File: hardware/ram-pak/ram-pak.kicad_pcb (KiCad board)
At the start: 4 copper layers, 29 x 18.1 mm, 23 parts, among them J1 PinHeader_2x22_P1.27mm, U1 TLV62568DBV, U2 S70KL1281, U3 S70KL1281

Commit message: Added missing 3d models.
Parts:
- J1: footprint pkl_pin_headers:PinHeader_2x22_P1.27mm_Vertical_Pass-Through__SMD -> pkl_pin_sockets:PinSocket_2x22_P1.27mm_Vertical_Pass-Through__SMD

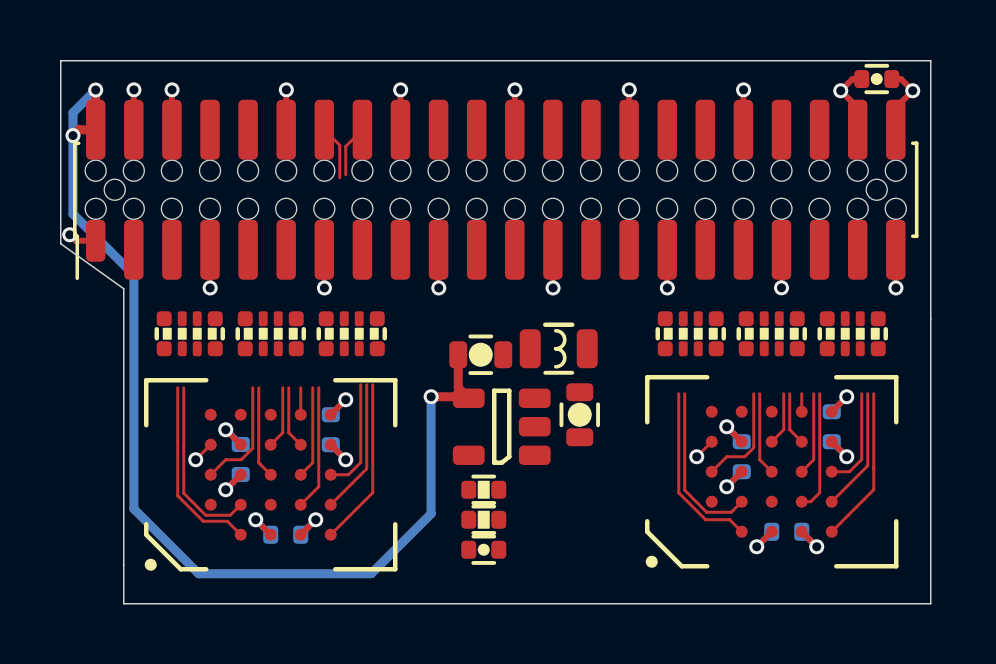
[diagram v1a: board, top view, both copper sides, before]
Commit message: Ram-Pak: Routed and length matched.
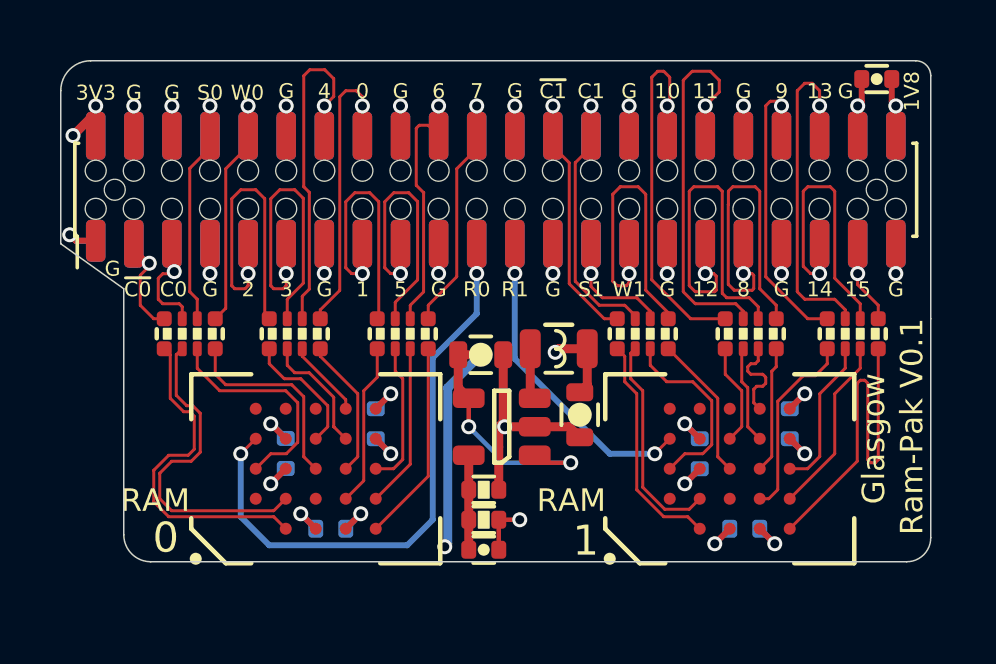
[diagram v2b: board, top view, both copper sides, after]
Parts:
- moved R3 1.70 mm to (36.9, 34.8)
- moved R4 1.60 mm to (44.9, 34.8)
- moved C5 1.51 mm to (34.5, 41.3)
- moved C6 1.51 mm to (36.0, 37.8)
- moved C7 1.51 mm to (33.0, 38.8)
- moved U2 1.51 mm to (34.0, 39.3)
- moved C10 1.40 mm to (46.8, 38.8)
- moved C8 1.40 mm to (48.3, 41.3)
- moved C9 1.40 mm to (49.8, 37.8)
- moved U3 1.40 mm to (47.8, 39.3)
- moved R2 0.80 mm to (33.3, 34.8)
- moved R5 0.70 mm to (48.5, 34.8)
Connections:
- net /CK0 renamed /CK0_P
- net /CK1 renamed /CK1_P
- net /Z0_N renamed /DQ15x
- net /Z0_P renamed /DQ14x
- net /Z10_N renamed /DQ3x
- net /Z10_P renamed /DQ2x
- net /Z11_N renamed /CK0x_N
- net /Z11_P renamed /CK0x_P
- net /Z12_N renamed /RWDS0x
- net /Z12_P renamed /~CS0x
- net /Z1_N renamed /DQ9x
- net /Z1_P renamed /DQ13x
- net /Z2_N renamed /DQ12x
- net /Z2_P renamed /DQ8x
- net /Z3_N renamed /RWDS1x
- net /Z3_P renamed /~CS1x
- net /Z4_N renamed /DQ11x
- net /Z4_P renamed /DQ10x
- net /Z5_N renamed /CK1x_N
- net /Z5_P renamed /CK1x_P
- net /Z6_N renamed /~RESET1
- net /Z6_P renamed /~RESET0
- net /Z7_N renamed /DQ6x
- net /Z7_P renamed /DQ7x
- net /Z8_N renamed /DQ5x
- net /Z8_P renamed /DQ1x
- net /Z9_N renamed /DQ4x
- net /Z9_P renamed /DQ0x
- net /~CK0 renamed /CK0_N
- net /~CK1 renamed /CK1_N
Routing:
- net /~RESET0: track 0.71 -> 20.5 mm, vias 1 -> 2
- net GND: track 30.1 -> 45.5 mm, vias 22 -> 23
- net /DQ12x: track 0.00 -> 14.4 mm, vias 0 -> 1
- net /DQ11x: track 0.00 -> 14.1 mm, vias 0 -> 1
- net /DQ10x: track 0.00 -> 13.9 mm, vias 0 -> 1
- net /RWDS1x: track 0.00 -> 12.6 mm, vias 0 -> 1
- net /DQ8x: track 0.00 -> 12.5 mm, vias 0 -> 1
- net /DQ13x: track 0.00 -> 12.3 mm, vias 0 -> 1
- net /DQ3x: track 0.00 -> 11.5 mm, vias 0 -> 1
- net /DQ2x: track 0.00 -> 11.3 mm, vias 0 -> 1
- net /DQ9x: track 0.00 -> 11.0 mm, vias 0 -> 1
- net /DQ14x: track 0.00 -> 10.9 mm, vias 0 -> 1
- net /DQ4x: track 1.81 -> 12.5 mm, vias 0 -> 1
- net /~RESET1: track 0.71 -> 11.3 mm, vias 1 -> 2
- net /DQ6x: track 0.00 -> 10.2 mm, vias 0 -> 1
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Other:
- board size 29 x 18.1 mm -> 29 x 16.7 mm
- board text added: "0"
- board text added: "1"
- board text added: "10"
- board text added: "11"
- board text added: "12"
- board text added: "13"
- board text added: "14"
- board text added: "15"
- board text added: "1V8"
- board text added: "2"
- board text added: "3"
- board text added: "3V3"
- board text added: "4"
- board text added: "5"
- board text added: "6"
- board text added: "7"
- board text added: "8"
- board text added: "9"
- board text added: "C0"
- board text added: "C1"
- board text added: "G"
- board text added: "Glasgow"
- board text added: "R0"
- board text added: "R1"
- board text added: "RAM"
- board text added: "Ram-Pak V0.1"
- board text added: "S0"
- board text added: "S1"
- board text added: "W0"
- board text added: "W1"
- board text added: "~C0"
- board text added: "~C1"

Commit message: ram-pak: silkscreen improvements.
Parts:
- added REF**: null_Logo_SilkS_5mm, pkl_logos:null_Logo_SilkS_5mm, B.Cu at (41.1, 37.3)
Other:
- board text added: "1B2 (C) 2021 CC-BY-SA 4.0"
- board text added: "Glasgow Ram-Pak V0.1"
- board text added: "NULL"

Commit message: ram-pak: Some more silkscreen work.
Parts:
- moved C7 0.50 mm to (32.5, 38.8)
- moved C10 0.50 mm to (46.3, 38.8)
- moved C5 0.50 mm to (34.5, 40.8)
- moved C6 0.50 mm to (36.5, 37.8)
- moved C8 0.50 mm to (48.3, 41.8)
- moved C9 0.50 mm to (50.3, 37.8)
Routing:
- net GND: track 45.5 -> 44.3 mm
- net +1V8: track 15.6 -> 14.4 mm
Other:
- board text added: "1B2(C)2021 CC-BY-SA"
- board text added: "Glasgow Ram-Pak V0.1a"
- board text added: "Ram-Pak V0.1a"
- board text removed: "Glasgow Ram-Pak V0.1"
- board text removed: "Ram-Pak V0.1"

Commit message: ram-pak: Fab layer placement plan cleanup.
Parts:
- moved REF** 0.20 mm to (40.9, 37.3)

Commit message: ram-pak: Extended and updated BOM information.
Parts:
- U2, U3: value S70KL1281 -> W957D8MFYA5I

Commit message: ram-pak: Removed back pads, added VSKIP bumped version.
* Removed the back side connector mounting pads. (only needed for the
  first prototype using 1.6mm thick pcb)
* Added VSKIP that allows the use of 3v3 RAM chips.
* Bumped version to V0.1b
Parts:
- added J2: pkl_jumper, pkl_jumpers:J_0603, B.Cu at (37.5, 41.2)
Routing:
- net GND: track 44.3 -> 28.6 mm
- net /~RESET0: track 20.5 -> 18.4 mm
- net /RWDS0x: track 8.55 -> 6.55 mm, vias 1 -> 0
- net /CK1x_P: track 10.1 -> 8.07 mm, vias 1 -> 0
- net /~CS0x: track 8.47 -> 6.48 mm, vias 1 -> 0
- net /DQ7x: track 8.96 -> 6.97 mm, vias 1 -> 0
- net /DQ6x: track 10.2 -> 8.18 mm, vias 1 -> 0
- net /CK1x_N: track 9.86 -> 7.87 mm, vias 1 -> 0
- net /~RESET1: track 11.3 -> 10.1 mm
- net /CK0x_P: track 4.60 -> 3.51 mm, vias 1 -> 0
- net /DQ9x: track 11.0 -> 9.98 mm, vias 1 -> 0
- net /DQ4x: track 12.5 -> 11.5 mm, vias 1 -> 0
- net /DQ13x: track 12.3 -> 11.3 mm, vias 1 -> 0
- net /DQ11x: track 14.1 -> 13.1 mm, vias 1 -> 0
- net /DQ10x: track 13.9 -> 12.9 mm, vias 1 -> 0
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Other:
- board text added: "Glasgow Ram-Pak V0.1b"
- board text added: "Ram-Pak V0.1b"
- board text added: "VSKIP"
- board text removed: "Glasgow Ram-Pak V0.1a"
- board text removed: "Ram-Pak V0.1a"

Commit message: ram-pak: VSKIP jumper position adjusted.
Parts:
- moved J2 0.60 mm to (36.9, 41.2)
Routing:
- net /~RESET0: track 18.4 -> 19.1 mm
- net +3V3: track 43.4 -> 44.0 mm
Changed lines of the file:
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@@
     (thickness 0.6)
     (drawings 619)
-    (tracks 534)
+    (tracks 540)
     (zones 0)
     (modules 25)
@@
     (add_net "Net-(U3-PadC5)")
   )
+  (module pkl_logos:null_Logo_SilkS_5mm (layer B.Cu)
+    (at 40.9 37.3 180)
+    (attr virtual)
+    (fp_text reference REF** (at 0 -4.55) (layer B.Fab) hide
+      (effects (font (size 1 1) (thickness 0.15)) (justify mirror))
+    )
+    (fp_text value null_Logo_SilkS_5mm (at 0 4.55) (layer B.Fab) hide
+      (effects (font (size 1 1) (thickness 0.15)) (justify mirror))
+    )
+    (fp_arc (start -0.4 -0.2) (end -0.7 -0.2) (angle 180) (layer B.SilkS) (width 0.15))
+    (fp_line (start 1 -0.5) (end 1.5 -0.5) (layer B.SilkS) (width 0.15))
+    (fp_line (start 1 0.5) (end 1 -0.5) (layer B.SilkS) (width 0.15))
+    (fp_line (start 0.2 -0.5) (end 0.7 -0.5) (layer B.SilkS) (width 0.15))
+    (fp_line (start 0.2 0.5) (end 0.2 -0.5) (layer B.SilkS) (width 0.15))
+    (fp_line (start -0.1 0.5) (end -0.1 -0.2) (layer B.SilkS) (width 0.15))
+    (fp_line (start -0.7 0.5) (end -0.7 -0.2) (layer B.SilkS) (width 0.15))
+    (fp_line (start -1 -0.5) (end -1 0.5) (layer B.SilkS) (width 0.15))
+    (fp_line (start -1.5 0.5) (end -1 -0.5) (layer B.SilkS) (width 0.15))
+    (fp_line (start -1.5 -0.5) (end -1.5 0.5) (layer B.SilkS) (width 0.15))
+    (fp_line (start 2.5 2.5) (end -2.5 2.5) (layer B.SilkS) (width 0.2))
+    (fp_line (start -2.5 2.5) (end -2.5 -2.5) (layer B.SilkS) (width 0.2))
+    (fp_line (start 2.5 2.5) (end 2.5 -2.5) (layer B.SilkS) (width 0.2))
+    (fp_line (start -2.5 -2.5) (end 2.5 -2.5) (layer B.SilkS) (width 0.2))
+  )
   (module pkl_jumpers:J_0603 (layer B.Cu)
-    (at 37.5 41.2 90)
+    (at 36.9 41.2 90)
     (descr "Jumper SMD 0603, reflow soldering")
     (tags "jumper 0603")
@@
     )
   )
-  (module pkl_logos:null_Logo_SilkS_5mm (layer B.Cu)
-    (at 40.9 37.3 180)
-    (attr virtual)
-    (fp_text reference REF** (at 0 -4.55) (layer B.Fab) hide
-      (effects (font (size 1 1) (thickness 0.15)) (justify mirror))
-    )
-    (fp_text value null_Logo_SilkS_5mm (at 0 4.55) (layer B.Fab) hide
-      (effects (font (size 1 1) (thickness 0.15)) (justify mirror))
-    )
-    (fp_line (start -2.5 -2.5) (end 2.5 -2.5) (layer B.SilkS) (width 0.2))
-    (fp_line (start 2.5 2.5) (end 2.5 -2.5) (layer B.SilkS) (width 0.2))
-    (fp_line (start -2.5 2.5) (end -2.5 -2.5) (layer B.SilkS) (width 0.2))
-    (fp_line (start 2.5 2.5) (end -2.5 2.5) (layer B.SilkS) (width 0.2))
-    (fp_line (start -1.5 -0.5) (end -1.5 0.5) (layer B.SilkS) (width 0.15))
-    (fp_line (start -1.5 0.5) (end -1 -0.5) (layer B.SilkS) (width 0.15))
-    (fp_line (start -1 -0.5) (end -1 0.5) (layer B.SilkS) (width 0.15))
-    (fp_line (start -0.7 0.5) (end -0.7 -0.2) (layer B.SilkS) (width 0.15))
-    (fp_line (start -0.1 0.5) (end -0.1 -0.2) (layer B.SilkS) (width 0.15))
-    (fp_line (start 0.2 0.5) (end 0.2 -0.5) (layer B.SilkS) (width 0.15))
-    (fp_line (start 0.2 -0.5) (end 0.7 -0.5) (layer B.SilkS) (width 0.15))
-    (fp_line (start 1 0.5) (end 1 -0.5) (layer B.SilkS) (width 0.15))
-    (fp_line (start 1 -0.5) (end 1.5 -0.5) (layer B.SilkS) (width 0.15))
-    (fp_arc (start -0.4 -0.2) (end -0.7 -0.2) (angle 180) (layer B.SilkS) (width 0.15))
-  )
   (module pkl_housings_bga:BGA-24_5x5_6.0x8.0mm locked (layer F.Cu)
     (at 47.8 39.3 90)
@@
     )
   )
-  (gr_text VSKIP (at 35.1 41.9) (layer B.SilkS)
+  (gr_text VSKIP (at 34.5 41.9) (layer B.SilkS)
     (effects (font (size 0.75 0.75) (thickness 0.15)) (justify mirror))
   )
@@
   (via (at 39.500006 35.5) (size 0.5) (drill 0.3) (layers F.Cu B.Cu) (net 2))
   (via (at 38.3 41.9) (size 0.5) (drill 0.3) (layers F.Cu B.Cu) (net 2))
-  (segment (start 38.4 36.600006) (end 39.500006 35.5) (width 0.3) (layer B.Cu) (net 2))
-  (segment (start 38.4 41.8) (end 38.4 36.600006) (width 0.3) (layer B.Cu) (net 2))
-  (segment (start 38.3 41.9) (end 38.4 41.8) (width 0.3) (layer B.Cu) (net 2))
   (via (at 26.665 27.20602) (size 0.5) (drill 0.3) (layers F.Cu B.Cu) (net 2))
   (segment (start 25.908 28.194) (end 26.665 27.437) (width 0.3) (layer In2.Cu) (net 2))
@@
   (segment (start 26.665 27.437) (end 26.665 27.20602) (width 0.3) (layer F.Cu) (net 2))
   (segment (start 26.665 27.437) (end 26.665 27.20602) (width 0.3) (layer In2.Cu) (net 2))
+  (segment (start 36.455248 41.905537) (end 38.294463 41.905537) (width 0.3) (layer In2.Cu) (net 2))
+  (segment (start 38.3 41.9) (end 39.250007 40.949993) (width 0.3) (layer B.Cu) (net 2))
+  (segment (start 36.449711 41.9) (end 36.455248 41.905537) (width 0.3) (layer In2.Cu) (net 2))
+  (segment (start 39.250007 40.949993) (end 39.250007 35.749999) (width 0.3) (layer B.Cu) (net 2))
   (segment (start 27.94 40.64) (end 29.2 41.9) (width 0.3) (layer In2.Cu) (net 2))
-  (segment (start 29.2 41.9) (end 37.946447 41.9) (width 0.3) (layer In2.Cu) (net 2))
+  (segment (start 39.250007 35.749999) (end 39.500006 35.5) (width 0.3) (layer B.Cu) (net 2))
+  (segment (start 29.2 41.9) (end 36.449711 41.9) (width 0.3) (layer In2.Cu) (net 2))
+  (segment (start 25.908 30.808) (end 27.94 32.84) (width 0.3) (layer In2.Cu) (net 2))
   (segment (start 27.94 32.84) (end 27.94 40.64) (width 0.3) (layer In2.Cu) (net 2))
-  (segment (start 25.908 30.808) (end 27.94 32.84) (width 0.3) (layer In2.Cu) (net 2))
-  (segment (start 37.946447 41.9) (end 38.3 41.9) (width 0.3) (layer In2.Cu) (net 2))
   (segment (start 25.908 28.194) (end 25.908 30.808) (width 0.3) (layer In2.Cu) (net 2))
-  (segment (start 37.625 41.9) (end 37.5 41.775) (width 0.3) (layer B.Cu) (net 2))
-  (segment (start 38.3 41.9) (end 37.625 41.9) (width 0.3) (layer B.Cu) (net 2))
+  (segment (start 38.294463 41.905537) (end 38.3 41.9) (width 0.3) (layer In2.Cu) (net 2))
+  (segment (start 37.025 41.9) (end 36.9 41.775) (width 0.3) (layer B.Cu) (net 2))
+  (segment (start 38.3 41.9) (end 37.025 41.9) (width 0.3) (layer B.Cu) (net 2))
   (via (at 36.5 38.8) (size 0.5) (drill 0.3) (layers F.Cu B.Cu) (net 3))
   (segment (start 36.5 38.8) (end 36 38.3) (width 0.2) (layer F.Cu) (net 3))
@@
   (segment (start 43.05 35.3) (end 42.5 35.3) (width 0.3) (layer F.Cu) (net 3))
   (segment (start 42.5 35.3) (end 42.3 35.5) (width 0.3) (layer F.Cu) (net 3))
-  (via (at 36.8 41.2) (size 0.5) (drill 0.3) (layers F.Cu B.Cu) (net 3))
-  (segment (start 37.375 40.625) (end 36.8 41.2) (width 0.3) (layer B.Cu) (net 3))
-  (segment (start 37.5 40.625) (end 37.375 40.625) (width 0.3) (layer B.Cu) (net 3))
+  (via (at 38 40) (size 0.5) (drill 0.3) (layers F.Cu B.Cu) (net 3))
+  (segment (start 37.375 40.625) (end 38 40) (width 0.3) (layer B.Cu) (net 3))
+  (segment (start 36.9 40.625) (end 37.375 40.625) (width 0.3) (layer B.Cu) (net 3))
   (segment (start 33.55 35.55) (end 35 37) (width 0.1) (layer F.Cu) (net 4))
   (segment (start 33.55 35.3) (end 33.55 35.55) (width 0.1) (layer F.Cu) (net 4))
@@
   (via (at 39.365 32.79) (size 0.5) (drill 0.3) (layers F.Cu B.Cu) (net 48))
   (segment (start 39.365 32) (end 39.365 32.79) (width 0.2) (layer F.Cu) (net 48))
-  (segment (start 37.9 35.6) (end 39.365 34.135) (width 0.2) (layer B.Cu) (net 48))
-  (segment (start 37.9 39.1) (end 37.9 35.6) (width 0.2) (layer B.Cu) (net 48))
-  (segment (start 35.15001 41.84999) (end 37.9 39.1) (width 0.2) (layer B.Cu) (net 48))
-  (segment (start 32.44999 41.84999) (end 35.15001 41.84999) (width 0.2) (layer B.Cu) (net 48))
+  (segment (start 31.499992 38.8) (end 31.499992 40.899992) (width 0.2) (layer B.Cu) (net 48))
+  (segment (start 32.44999 41.84999) (end 35.45001 41.84999) (width 0.2) (layer B.Cu) (net 48))
   (segment (start 31.499992 40.899992) (end 32.44999 41.84999) (width 0.2) (layer B.Cu) (net 48))
   (segment (start 39.365 34.135) (end 39.365 32.79) (width 0.2) (layer B.Cu) (net 48))
-  (segment (start 31.499992 38.8) (end 31.499992 40.899992) (width 0.2) (layer B.Cu) (net 48))
+  (segment (start 35.45001 41.84999) (end 36 41.3) (width 0.2) (layer B.Cu) (net 48))
+  (segment (start 36 41.3) (end 36 40.1) (width 0.2) (layer B.Cu) (net 48))
+  (segment (start 36 40.1) (end 36.4 39.7) (width 0.2) (layer B.Cu) (net 48))
+  (segment (start 36.4 39.7) (end 37.3 39.7) (width 0.2) (layer B.Cu) (net 48))
+  (segment (start 37.3 39.7) (end 37.9 39.1) (width 0.2) (layer B.Cu) (net 48))
+  (segment (start 37.9 39.1) (end 37.9 35.6) (width 0.2) (layer B.Cu) (net 48))
+  (segment (start 37.9 35.6) (end 39.365 34.135) (width 0.2) (layer B.Cu) (net 48))
   (segment (start 38.095 28.605) (end 38.095 28) (width 0.1) (layer F.Cu) (net 49))
   (segment (start 37.745 27.85) (end 38.095 28.2) (width 0.1) (layer F.Cu) (net 49))
